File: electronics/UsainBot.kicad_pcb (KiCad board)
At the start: 2 copper layers, 176 x 198 mm, 2 parts

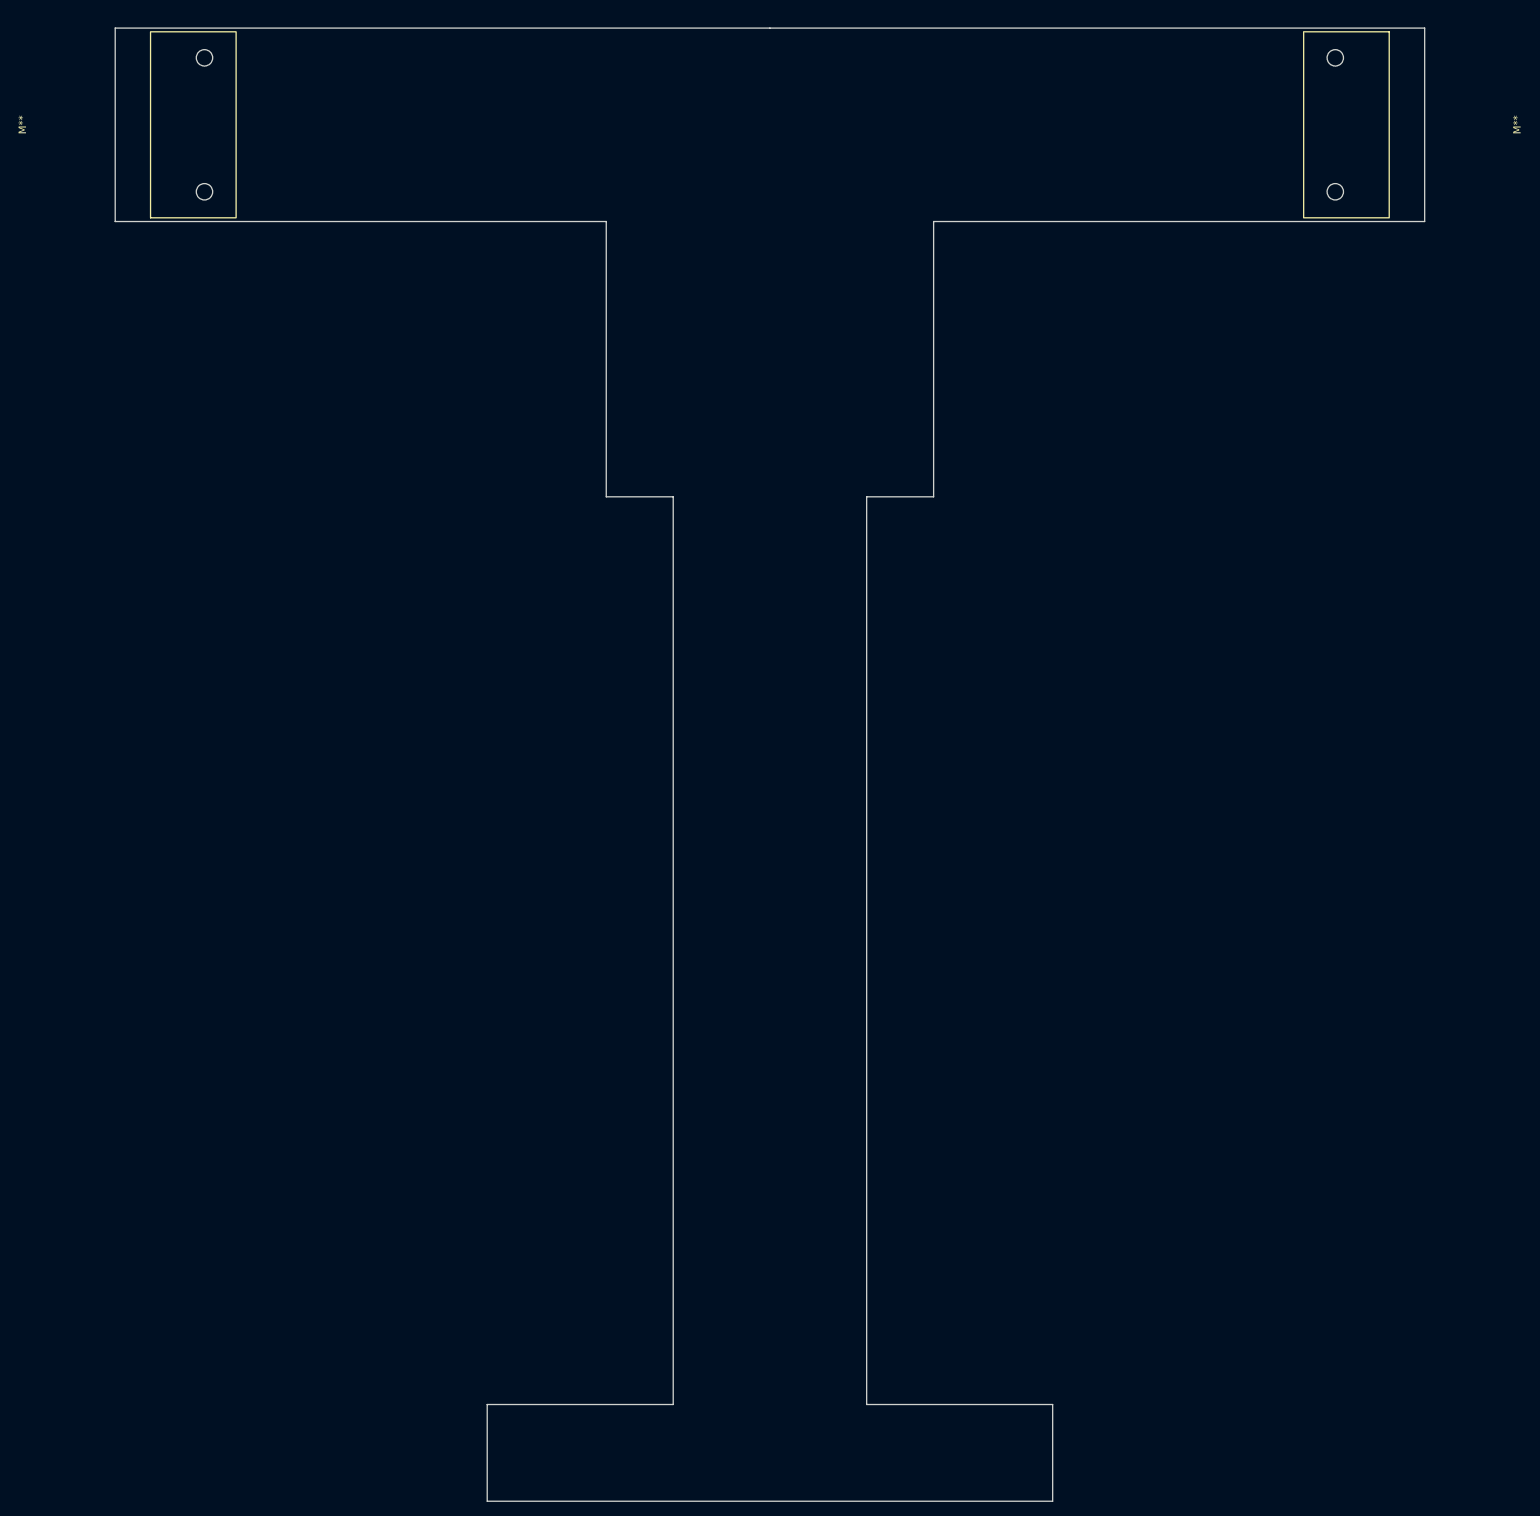
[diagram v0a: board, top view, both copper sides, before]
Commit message: Pose les 335 composants sur la carte, chacun contre l'actif qu'il sert
Le PCB ne portait que le contour. Il porte maintenant tout le schéma, placé
par script : la position de chaque composant est écrite dans `layout.py`,
jamais posée à la souris. Les rangées de résistances alignées loin de leur
circuit ont disparu ; à leur place une grappe par fonction, au contact du
boîtier. Ce qui ne pouvait pas suivre — les passifs lents des deux ponts en
H, coincés derrière l'équerre moteur — est regroupé en un bloc unique plutôt
que dispersé.

Six zones sur 194 × 155 mm. L'arrière, seule bande libre devant les
équerres, prend les ponts en H aux deux angles, le chargeur, l'USB et le
trio d'alimentation : XT30 vertical, nappe d'équilibrage, et les deux gros
perçages où se soudent les fils de l'ESC, qui se dresse sur la tranche
juste au-dessus. Le couloir entre les équerres et le trou de turbine reçoit
la centrale inertielle, au plus près du centre de rotation. Les épaules
portent le convertisseur 3,3 V — descendu là, il ne mange plus la bande
arrière —, l'interrupteur général et la station de télémétrie à 75°. L'IHM
place l'écran sur entretoises et le LQFP144 à 45° dessous, son découplage
logé dans les quatre poches entre le losange du boîtier et les bords du
module ; manettes à gauche, télémètres à droite, parce qu'on regarde l'écran
par l'arrière. Le nez enfin garde la passerelle centrale pour la station à
15°, la moustache et ses passifs étant passés dessous, contre les capteurs.

Une exception au tout-script, et elle prime : une empreinte verrouillée dans
pcbnew est une décision prise à l'écran, sur la pièce réelle. `lock_import.py`
les relève dans `locked.json`, que `layout.py` applique par-dessus sa propre
table ; `place_pcb.py` ne les efface pas au `--reset` et ne les déplace
jamais. Il rafraîchit en revanche leur dessin d'empreinte sur place —
verrouiller fige où l'on est, pas la version du plan. C'est ainsi que le
module OLED a suivi la correction d'entraxe sans bouger d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
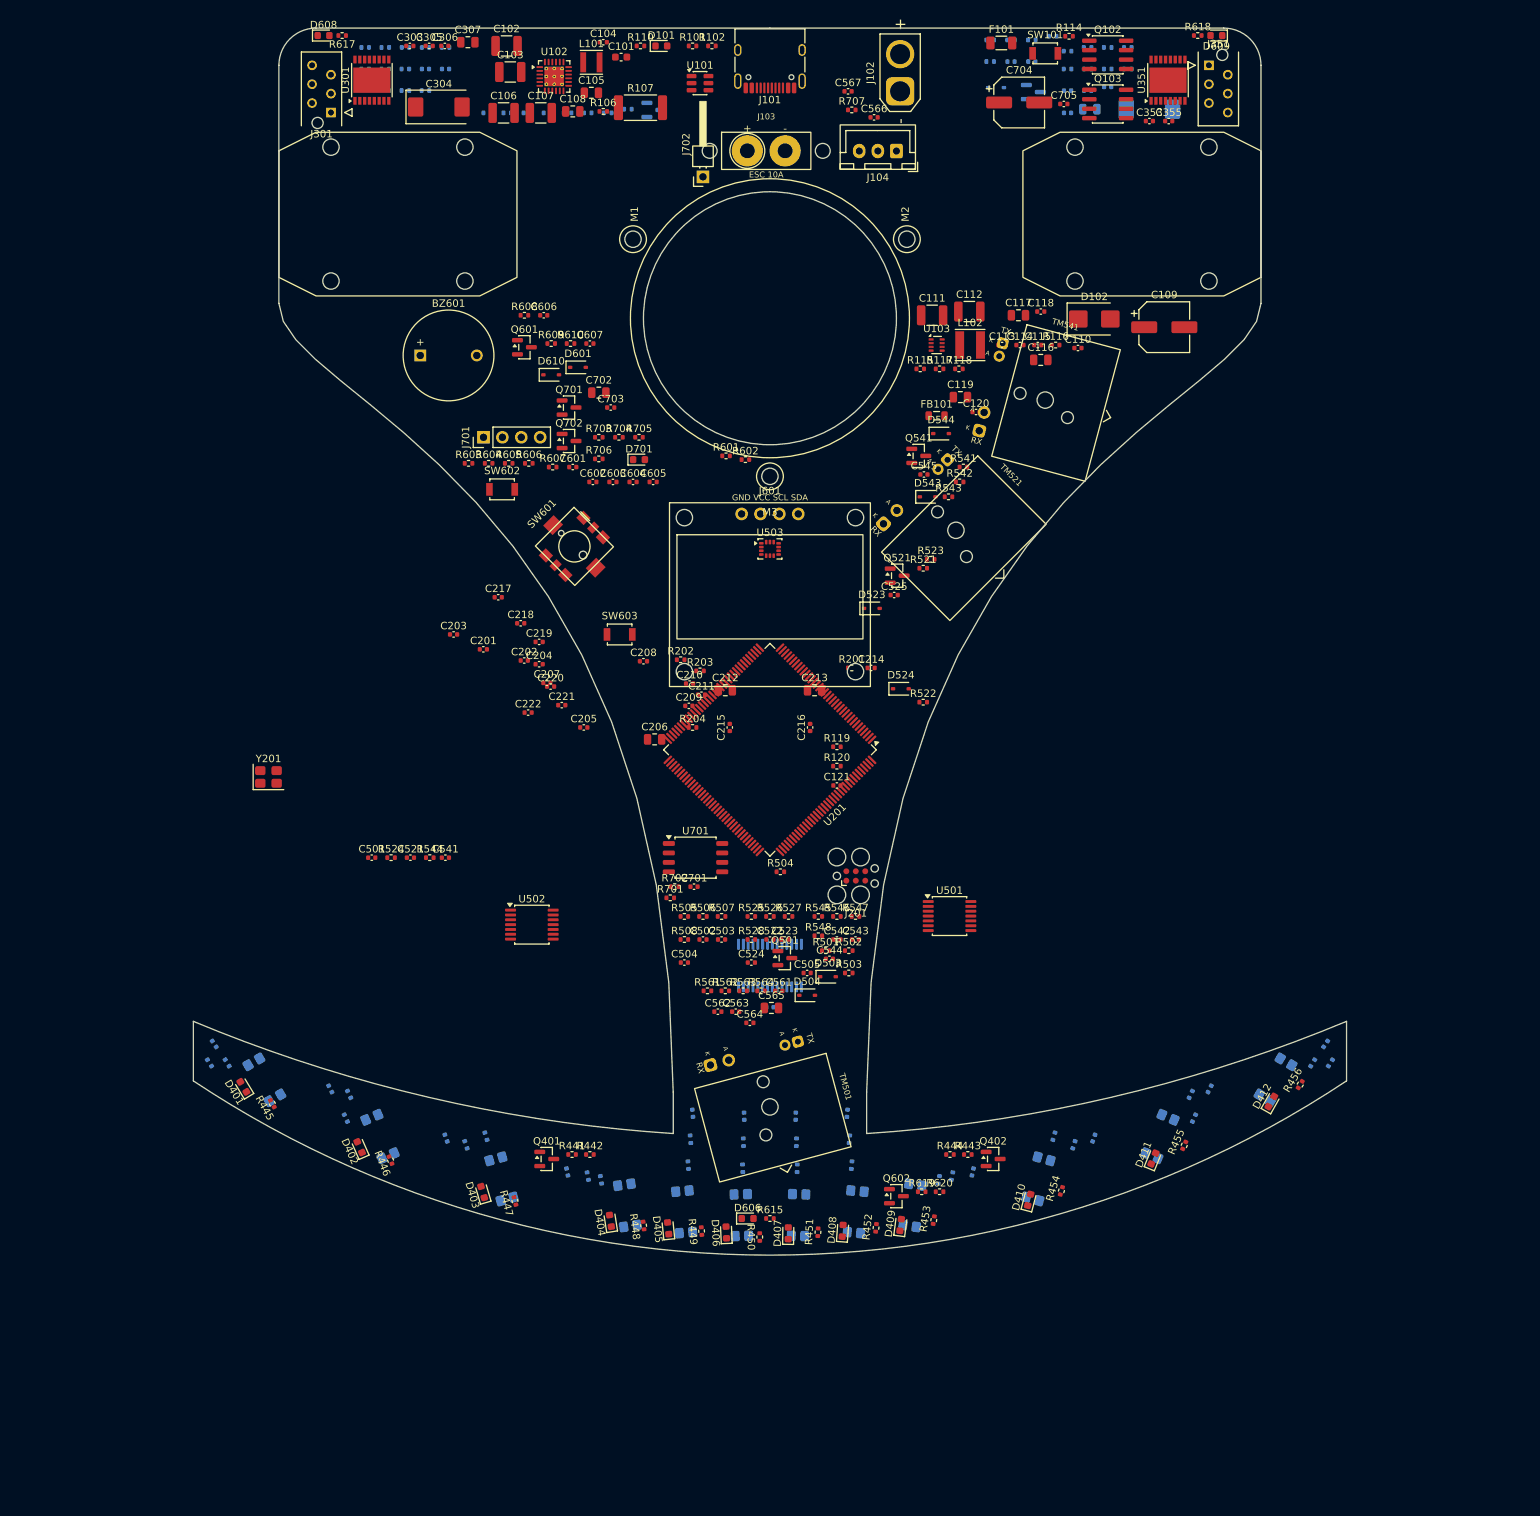
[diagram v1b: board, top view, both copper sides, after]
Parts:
- removed M** (x2): GM12-N20, Pacabot:Motor_GM12-N20_Bracket
- added BZ601: buzzer magnetique 9 x 5,5 mm, MagneticBuzzer_ProSignal_ABI-009-RC, F.Cu at (108.0, 164.0)
- added C101: 1uF, C_0603_1608Metric, F.Cu at (135.0, 123.9)
- added C102: 22uF, C_1210_3225Metric, F.Cu at (119.6, 122.4)
- added C103: 22uF, C_1210_3225Metric, F.Cu at (120.1, 125.9)
- added C104: 47nF, C_0402_1005Metric, F.Cu at (132.6, 121.9)
- added C105: 4u7F, C_0805_2012Metric, F.Cu at (131.0, 128.7)
- added C106: 22uF, C_1210_3225Metric, F.Cu at (119.2, 131.4)
- added C107: 22uF, C_1210_3225Metric, F.Cu at (124.2, 131.4)
- added C108: 10uF, C_0805_2012Metric, F.Cu at (128.5, 131.2)
- added C109: 100uF, CP_Elec_6.3x7.7, F.Cu at (208.0, 160.2)
- added C110: 100nF, C_0402_1005Metric, F.Cu at (196.4, 163.0)
- added C111: 10uF, C_1210_3225Metric, F.Cu at (176.8, 158.6)
- added C112: 10uF, C_1210_3225Metric, F.Cu at (181.8, 158.1)
- added C113: 100nF, C_0402_1005Metric, F.Cu at (186.2, 162.6)
- added C114: 100nF, C_0402_1005Metric, F.Cu at (188.6, 162.6)
- added C115: 10nF, C_0402_1005Metric, F.Cu at (191.0, 162.6)
- added C116: 22uF, C_0805_2012Metric, F.Cu at (191.4, 164.6)
- added C117: 22uF, C_0805_2012Metric, F.Cu at (188.4, 158.6)
- added C118: 100nF, C_0402_1005Metric, F.Cu at (191.4, 158.1)
- added C119: 10uF, C_0805_2012Metric, F.Cu at (180.6, 169.6)
- added C120: 100nF, C_0402_1005Metric, F.Cu at (182.7, 171.6)
- added C121: 100nF, C_0402_1005Metric, F.Cu at (164.0, 221.8)
- added C122: 100nF, C_0402_1005Metric, B.Cu at (187.4, 124.5)
- added C123: 1uF, C_0402_1005Metric, B.Cu at (190.2, 124.5)
- added C124: 100nF, C_0402_1005Metric, B.Cu at (155.0, 251.6)
- added C201: 100nF, C_0402_1005Metric, F.Cu at (116.5, 203.5)
- added C202: 100nF, C_0402_1005Metric, F.Cu at (122.0, 205.0)
- added C203: 100nF, C_0402_1005Metric, F.Cu at (112.5, 201.5)
- added C204: 100nF, C_0402_1005Metric, F.Cu at (124.0, 205.5)
- added C205: 100nF, C_0402_1005Metric, F.Cu at (130.0, 214.0)
- added C206: 4u7F, C_0805_2012Metric, F.Cu at (139.5, 215.6)
- added C207: 100nF, C_0402_1005Metric, F.Cu at (125.0, 208.0)
- added C208: 100nF, C_0402_1005Metric, F.Cu at (138.0, 205.1)
- added C209: 1uF, C_0402_1005Metric, F.Cu at (144.1, 211.1)
- added C210: 100nF, C_0402_1005Metric, F.Cu at (144.2, 208.1)
- added C211: 1uF, C_0402_1005Metric, F.Cu at (145.8, 209.6)
- added C212: 2u2F, C_0805_2012Metric, F.Cu at (149.0, 209.0)
- added C213: 2u2F, C_0805_2012Metric, F.Cu at (161.0, 209.0)
- added C214: 100nF, C_0402_1005Metric, F.Cu at (168.6, 206.0)
- added C215: 10pF, C_0402_1005Metric, F.Cu at (149.6, 214.0)
- added C216: 10pF, C_0402_1005Metric, F.Cu at (160.4, 214.0)
- added C217: 100nF, C_0402_1005Metric, F.Cu at (118.5, 196.5)
- added C218: 100nF, C_0402_1005Metric, F.Cu at (121.5, 200.0)
- added C219: 100nF, C_0402_1005Metric, F.Cu at (124.0, 202.5)
- added C220: 100nF, C_0402_1005Metric, F.Cu at (125.5, 208.5)
- added C221: 100nF, C_0402_1005Metric, F.Cu at (127.0, 211.0)
- added C222: 100nF, C_0402_1005Metric, F.Cu at (122.5, 212.0)
- added C301: 100nF, C_0402_1005Metric, B.Cu at (106.0, 122.6)
- added C302: 1nF, C_0402_1005Metric, B.Cu at (108.7, 122.6)
- added C303: 100nF, C_0402_1005Metric, F.Cu at (106.6, 122.4)
- added C304: 100uF, CP_EIA-7343-20_Kemet-V, F.Cu at (110.5, 130.6)
- added C305: 100nF, C_0402_1005Metric, F.Cu at (109.2, 122.4)
- added C306: 22nF, C_0402_1005Metric, F.Cu at (111.3, 122.4)
- added C307: 100nF, C_0805_2012Metric, F.Cu at (114.4, 121.9)
- added C308: 1nF, C_0402_1005Metric, B.Cu at (108.7, 125.5)
- added C309: 1nF, C_0402_1005Metric, B.Cu at (111.4, 125.5)
- added C352: 1nF, C_0402_1005Metric, B.Cu at (195.0, 128.4)
- added C353: 100nF, C_0402_1005Metric, F.Cu at (206.0, 132.5)
- added C354: 100uF, CP_EIA-7343-20_Kemet-V, B.Cu at (206.0, 130.9)
- added C355: 100nF, C_0402_1005Metric, F.Cu at (208.6, 132.5)
- added C356: 22nF, C_0402_1005Metric, B.Cu at (195.0, 131.4)
- added C357: 100nF, C_0805_2012Metric, B.Cu at (198.0, 130.9)
- added C358: 1nF, C_0402_1005Metric, B.Cu at (197.7, 128.4)
- added C359: 1nF, C_0402_1005Metric, B.Cu at (200.4, 127.9)
- added C401: 1nF, C_0402_1005Metric, B.Cu at (80.3, 256.5)
- added C402: 1nF, C_0402_1005Metric, B.Cu at (95.9, 262.6)
- added C403: 1nF, C_0402_1005Metric, B.Cu at (111.5, 269.2)
- added C404: 1nF, C_0402_1005Metric, B.Cu at (127.8, 273.7)
- added C405: 1nF, C_0402_1005Metric, B.Cu at (144.6, 265.9)
- added C406: 1nF, C_0402_1005Metric, B.Cu at (151.5, 266.3)
- added C407: 1nF, C_0402_1005Metric, B.Cu at (158.5, 266.3)
- added C408: 1nF, C_0402_1005Metric, B.Cu at (165.4, 265.9)
- added C409: 1nF, C_0402_1005Metric, B.Cu at (182.2, 273.7)
- added C410: 1nF, C_0402_1005Metric, B.Cu at (198.5, 269.2)
- added C411: 1nF, C_0402_1005Metric, B.Cu at (214.1, 262.6)
- added C412: 1nF, C_0402_1005Metric, B.Cu at (229.7, 256.5)
- added C501: 22pF, C_0402_1005Metric, F.Cu at (101.5, 231.5)
- added C502: 1nF, C_0402_1005Metric, F.Cu at (146.0, 242.5)
- added C503: 1uF, C_0402_1005Metric, F.Cu at (148.5, 242.5)
- added C504: 4n7, C_0402_1005Metric, F.Cu at (143.5, 245.6)
- added C505: 10nF, C_0402_1005Metric, F.Cu at (160.0, 247.0)
- added C521: 22pF, C_0402_1005Metric, F.Cu at (106.7, 231.5)
- added C522: 1nF, C_0402_1005Metric, F.Cu at (155.0, 242.5)
- added C523: 1uF, C_0402_1005Metric, F.Cu at (157.0, 242.5)
- added C524: 4n7, C_0402_1005Metric, F.Cu at (152.5, 245.6)
- added C525: 10nF, C_0402_1005Metric, F.Cu at (171.7, 196.2)
- added C541: 22pF, C_0402_1005Metric, F.Cu at (111.4, 231.5)
- added C542: 1nF, C_0402_1005Metric, F.Cu at (164.0, 242.5)
- added C543: 1uF, C_0402_1005Metric, F.Cu at (166.5, 242.5)
- added C544: 4n7, C_0402_1005Metric, F.Cu at (163.0, 245.1)
- added C545: 10nF, C_0402_1005Metric, F.Cu at (175.7, 180.0)
- added C561: 1uF, C_0402_1005Metric, F.Cu at (156.2, 249.4)
- added C562: 1uF, C_0402_1005Metric, F.Cu at (148.0, 252.2)
- added C563: 100nF, C_0402_1005Metric, F.Cu at (150.4, 252.2)
- added C564: 100nF, C_0402_1005Metric, F.Cu at (152.3, 253.7)
- added C565: 10uF, C_0805_2012Metric, F.Cu at (155.2, 251.7)
- added C566: 100nF, C_0402_1005Metric, F.Cu at (169.0, 132.0)
- added C567: 100nF, C_0402_1005Metric, F.Cu at (165.5, 128.5)
- added C601: 100nF, C_0402_1005Metric, F.Cu at (128.5, 179.0)
- added C602: 100nF, C_0402_1005Metric, F.Cu at (131.2, 181.0)
- added C603: 100nF, C_0402_1005Metric, F.Cu at (133.9, 181.0)
- added C604: 100nF, C_0402_1005Metric, F.Cu at (136.6, 181.0)
- added C605: 100nF, C_0402_1005Metric, F.Cu at (139.3, 181.0)
- added C606: 100nF, C_0402_1005Metric, F.Cu at (124.6, 158.6)
- added C607: 100nF, C_0402_1005Metric, F.Cu at (130.8, 162.4)
- added C701: 100nF, C_0402_1005Metric, F.Cu at (144.8, 235.4)
- added C702: 10uF, C_0805_2012Metric, F.Cu at (132.0, 169.0)
- added C703: 100nF, C_0402_1005Metric, F.Cu at (133.6, 171.0)
- added C704: 220uF, CP_Elec_6.3x7.7, F.Cu at (188.5, 130.0)
- added C705: 100nF, C_0402_1005Metric, F.Cu at (194.5, 130.2)
- added D101: vert - charge, LED_0603_1608Metric, F.Cu at (140.4, 122.4)
- added D102: SMBJ9.0A, D_SMB, F.Cu at (198.6, 159.1)
- added D106: BAT54, D_SOD-323, B.Cu at (185.4, 128.0)
- added D401: verte - capteur 00, LED_0603_1608Metric, F.Cu at (84.2, 262.3)
- added D402: verte - capteur 01, LED_0603_1608Metric, F.Cu at (99.9, 270.4)
- added D403: verte - capteur 02, LED_0603_1608Metric, F.Cu at (116.4, 276.4)
- added D404: verte - capteur 03, LED_0603_1608Metric, F.Cu at (133.6, 280.3)
- added D405: verte - capteur 04, LED_0603_1608Metric, F.Cu at (141.3, 281.3)
- added D406: verte - capteur 05, LED_0603_1608Metric, F.Cu at (149.1, 281.9)
- added D407: verte - capteur 06, LED_0603_1608Metric, F.Cu at (157.5, 282.0)
- added D408: verte - capteur 07, LED_0603_1608Metric, F.Cu at (164.8, 281.7)
- added D409: verte - capteur 08, LED_0603_1608Metric, F.Cu at (172.6, 280.9)
- added D410: verte - capteur 09, LED_0603_1608Metric, F.Cu at (189.8, 277.5)
- added D411: verte - capteur 10, LED_0603_1608Metric, F.Cu at (206.5, 271.9)
- added D412: verte - capteur 11, LED_0603_1608Metric, F.Cu at (222.4, 264.3)
- added D503: PESD3V3, D_SOD-323, F.Cu at (162.8, 247.5)
- added D504: BAT54, D_SOD-323, F.Cu at (160.0, 250.0)
- added D523: PESD3V3, D_SOD-323, F.Cu at (168.7, 198.0)
- added D524: BAT54, D_SOD-323, F.Cu at (172.6, 208.8)
- added D543: PESD3V3, D_SOD-323, F.Cu at (176.2, 183.0)
- added D544: BAT54, D_SOD-323, F.Cu at (178.0, 174.5)
- added D601: BAT54, D_SOD-323, F.Cu at (129.2, 165.6)
- added D606: bleue - nez, LED_0603_1608Metric, F.Cu at (152.0, 280.0)
- added D608: rouge - arriere, LED_0603_1608Metric, F.Cu at (95.0, 121.0)
- added D609: rouge - arriere, LED_0603_1608Metric, F.Cu at (215.0, 121.0)
- added D610: BAT54, D_SOD-323, F.Cu at (125.6, 166.6)
- added D701: bleue, LED_0603_1608Metric, F.Cu at (137.4, 178.0)
- added F101: 12 A, R_1206_3216Metric, F.Cu at (186.1, 122.0)
- added FB101: 600R @ 100 MHz, L_0805_2012Metric, F.Cu at (177.4, 172.1)
- added J101: TYPE-C-31-M-12, USB_C_Receptacle_HRO_TYPE-C-31-M-12, F.Cu at (155.0, 124.0)
- added J102: Pack 2S - puissance, AMASS_XT30U-M_1x02_P5.0mm_Vertical, F.Cu at (172.5, 128.5)
- added J103: MultiStar 10A (debout), Pacabot:ESC_Multistar_10A, F.Cu at (154.5, 136.5)
- added J104: Pack 2S - equilibrage, JST_XH_B3B-XH-A_1x03_P2.50mm_Vertical, F.Cu at (172.0, 136.5)
- added J201: TC2030-IDC-FP, Tag-Connect_TC2030-IDC-FP_2x03_P1.27mm_Vertical, F.Cu at (166.5, 234.0)
- added J301: Moteur Faulhaber + IE2, TE_Micro-MaTch_215079-6_2x03_P1.27mm_Vertical, F.Cu at (96.0, 131.3)
- added J351: Moteur Faulhaber + IE2, TE_Micro-MaTch_215079-6_2x03_P1.27mm_Vertical, F.Cu at (214.0, 125.0)
- added J601: OLED SSD1306 I2C, OLED_096_I2C, F.Cu at (155.0, 196.2)
- added J701: Module OTA (ESP32-C3), PinHeader_1x04_P2.54mm_Vertical, F.Cu at (116.5, 175.0)
- added J702: Signal ESC (coudee), PinHeader_1x01_P2.54mm_Horizontal, F.Cu at (146.0, 140.0)
- added L101: 1uH / 4 A, L_Taiyo-Yuden_NR-30xx, F.Cu at (131.0, 124.6)
- added L102: 4u7H / 3 A, L_Taiyo-Yuden_NR-40xx, F.Cu at (181.9, 162.6)
- added M1: Faulhaber 1524T006SR + IE2 + 15/10, Motor_Faulhaber_1524_15-10, F.Cu at (105.0, 145.0)
- added M2: Faulhaber 1524T006SR + IE2 + 15/10, Motor_Faulhaber_1524_15-10, F.Cu at (205.0, 145.0)
- added M3: Turbine_EDF27_dessus, Turbine_EDF27_dessus, F.Cu at (155.0, 159.0)
- added Q101: AO3400A, SOT-23, B.Cu at (139.4, 131.0)
- added Q102: AO4407A, SOIC-8_3.9x4.9mm_P1.27mm, F.Cu at (200.4, 123.6)
- added Q103: AO4407A, SOIC-8_3.9x4.9mm_P1.27mm, F.Cu at (200.4, 130.2)
- added Q104: AO3400A, SOT-23, B.Cu at (190.4, 128.6)
- added Q401: AO3400A, SOT-23, F.Cu at (125.0, 272.0)
- added Q402: AO3400A, SOT-23, F.Cu at (185.0, 272.0)
- added Q501: AO3400A, SOT-23, F.Cu at (157.0, 245.0)
- added Q521: AO3400A, SOT-23, F.Cu at (172.1, 193.6)
- added Q541: AO3400A, SOT-23, F.Cu at (175.0, 177.5)
- added Q601: AO3400A, SOT-23, F.Cu at (122.0, 162.9)
- added Q602: AO3400A, SOT-23, F.Cu at (172.0, 277.0)
- added Q701: SI2301CDS, SOT-23, F.Cu at (128.0, 171.0)
- added Q702: AO3400A, SOT-23, F.Cu at (128.0, 175.5)
- added R101: 5k1, R_0402_1005Metric, F.Cu at (144.6, 122.4)
- added R102: 5k1, R_0402_1005Metric, F.Cu at (147.2, 122.4)
- added R103: 383R, R_0402_1005Metric, B.Cu at (117.0, 131.4)
- added R104: 5k23, R_0402_1005Metric, B.Cu at (119.7, 131.4)
- added R105: 30k1, R_0402_1005Metric, B.Cu at (122.4, 131.4)
- added R106: 300R, R_0402_1005Metric, F.Cu at (132.6, 131.2)
- added R107: 10R, R_2512_6332Metric, F.Cu at (137.6, 130.7)
- added R108: 10k, R_0402_1005Metric, B.Cu at (125.1, 131.4)
- added R109: 10k, R_0402_1005Metric, B.Cu at (127.8, 131.4)
- added R110: 2k2, R_0402_1005Metric, F.Cu at (137.6, 122.4)
- added R111: 100k, R_0402_1005Metric, B.Cu at (130.5, 131.4)
- added R112: 100R, R_0402_1005Metric, B.Cu at (133.2, 131.4)
- added R113: 100k, R_0402_1005Metric, B.Cu at (135.9, 130.9)
- added R114: 100k, R_0402_1005Metric, F.Cu at (195.2, 121.1)
- added R115: 100k, R_0402_1005Metric, F.Cu at (175.2, 165.8)
- added R116: 42k2, R_0402_1005Metric, F.Cu at (193.4, 162.6)
- added R117: 100k, R_0402_1005Metric, F.Cu at (177.8, 165.8)
- added R118: 31k6, R_0402_1005Metric, F.Cu at (180.4, 165.8)
- added R119: 22k, R_0402_1005Metric, F.Cu at (164.0, 216.6)
- added R120: 10k, R_0402_1005Metric, F.Cu at (164.0, 219.2)
- added R124: 100R, R_0402_1005Metric, B.Cu at (184.6, 121.6)
- added R125: 10k, R_0402_1005Metric, B.Cu at (187.4, 121.6)
- added R126: 100k, R_0402_1005Metric, B.Cu at (190.2, 121.6)
- added R127: 470k, R_0402_1005Metric, B.Cu at (193.0, 121.1)
- added R128: 220k, R_0402_1005Metric, B.Cu at (184.6, 124.5)
- added R201: 10k, R_0402_1005Metric, F.Cu at (166.0, 206.0)
- added R202: 10k, R_0402_1005Metric, F.Cu at (143.0, 204.9)
- added R203: 10k, R_0402_1005Metric, F.Cu at (145.6, 206.4)
- added R204: 220R, R_0402_1005Metric, F.Cu at (144.6, 214.0)
- added R301: 10k, R_0402_1005Metric, B.Cu at (100.6, 122.6)
- added R302: 6k8, R_0402_1005Metric, B.Cu at (103.3, 122.6)
- added R303: 100k, R_0402_1005Metric, B.Cu at (111.4, 122.6)
- added R304: 10k, R_0402_1005Metric, B.Cu at (100.6, 125.5)
- added R305: 20k, R_0402_1005Metric, B.Cu at (103.3, 125.5)
- added R306: 10k, R_0402_1005Metric, B.Cu at (106.0, 125.5)
- added R307: 1k, R_0402_1005Metric, B.Cu at (100.6, 128.4)
- added R308: 100R, R_0402_1005Metric, B.Cu at (103.3, 128.4)
- added R309: 100R, R_0402_1005Metric, B.Cu at (106.0, 128.4)
- added R310: 100R, R_0402_1005Metric, B.Cu at (108.7, 128.4)
- added R353: 100k, R_0402_1005Metric, B.Cu at (195.0, 123.1)
- added R354: 10k, R_0402_1005Metric, B.Cu at (197.7, 122.6)
- added R355: 20k, R_0402_1005Metric, B.Cu at (200.4, 122.6)
- added R356: 10k, R_0402_1005Metric, B.Cu at (203.1, 122.6)
- added R357: 1k, R_0402_1005Metric, B.Cu at (195.0, 125.5)
- added R358: 100R, R_0402_1005Metric, B.Cu at (197.7, 125.5)
- added R359: 100R, R_0402_1005Metric, B.Cu at (200.4, 125.5)
- added R360: 100R, R_0402_1005Metric, B.Cu at (203.1, 125.5)
- added R401: 100R, R_0402_1005Metric, B.Cu at (82.0, 259.1)
- added R402: 100R, R_0402_1005Metric, B.Cu at (98.0, 266.5)
- added R403: 100R, R_0402_1005Metric, B.Cu at (116.8, 268.9)
- added R404: 100R, R_0402_1005Metric, B.Cu at (132.3, 274.8)
- added R405: 100R, R_0402_1005Metric, B.Cu at (144.0, 272.8)
- added R406: 100R, R_0402_1005Metric, B.Cu at (151.3, 273.2)
- added R407: 100R, R_0402_1005Metric, B.Cu at (158.7, 273.2)
- added R408: 100R, R_0402_1005Metric, B.Cu at (166.0, 272.8)
- added R409: 100R, R_0402_1005Metric, B.Cu at (177.7, 274.8)
- added R410: 100R, R_0402_1005Metric, B.Cu at (193.2, 268.9)
- added R411: 100R, R_0402_1005Metric, B.Cu at (212.0, 266.5)
- added R412: 100R, R_0402_1005Metric, B.Cu at (227.9, 259.1)
- added R421: 10k, R_0402_1005Metric, B.Cu at (79.7, 259.1)
- added R422: 10k, R_0402_1005Metric, B.Cu at (98.4, 263.3)
- added R423: 10k, R_0402_1005Metric, B.Cu at (114.1, 270.1)
- added R424: 10k, R_0402_1005Metric, B.Cu at (130.5, 274.3)
- added R425: 10k, R_0402_1005Metric, B.Cu at (144.3, 269.3)
- added R426: 10k, R_0402_1005Metric, B.Cu at (151.4, 269.7)
- added R427: 10k, R_0402_1005Metric, B.Cu at (158.6, 269.7)
- added R428: 10k, R_0402_1005Metric, B.Cu at (165.7, 269.3)
- added R429: 10k, R_0402_1005Metric, B.Cu at (179.5, 274.3)
- added R430: 10k, R_0402_1005Metric, B.Cu at (195.9, 270.1)
- added R431: 10k, R_0402_1005Metric, B.Cu at (211.6, 263.3)
- added R432: 10k, R_0402_1005Metric, B.Cu at (230.3, 259.1)
- added R441: 100R, R_0402_1005Metric, F.Cu at (128.4, 271.4)
- added R442: 100k, R_0402_1005Metric, F.Cu at (130.8, 271.4)
- added R443: 100R, R_0402_1005Metric, F.Cu at (181.6, 271.4)
- added R444: 100k, R_0402_1005Metric, F.Cu at (179.2, 271.4)
- added R445: 1k, R_0402_1005Metric, F.Cu at (88.1, 264.6)
- added R446: 1k, R_0402_1005Metric, F.Cu at (104.0, 272.2)
- added R447: 1k, R_0402_1005Metric, F.Cu at (120.7, 277.6)
- added R448: 1k, R_0402_1005Metric, F.Cu at (138.0, 280.9)
- added R449: 1k, R_0402_1005Metric, F.Cu at (145.8, 281.7)
- added R450: 1k, R_0402_1005Metric, F.Cu at (153.6, 282.5)
- added R451: 1k, R_0402_1005Metric, F.Cu at (161.5, 281.8)
- added R452: 1k, R_0402_1005Metric, F.Cu at (169.3, 281.3)
- added R453: 1k, R_0402_1005Metric, F.Cu at (177.0, 280.2)
- added R454: 1k, R_0402_1005Metric, F.Cu at (194.2, 276.3)
- added R455: 1k, R_0402_1005Metric, F.Cu at (210.7, 270.2)
- added R456: 1k, R_0402_1005Metric, F.Cu at (226.3, 262.0)
- added R501: 100R, R_0402_1005Metric, F.Cu at (162.5, 244.0)
- added R502: 100R, R_0402_1005Metric, F.Cu at (165.6, 244.0)
- added R503: 100k, R_0402_1005Metric, F.Cu at (165.6, 247.0)
- added R504: 220k, R_0402_1005Metric, F.Cu at (156.4, 233.4)
- added R505: 100k, R_0402_1005Metric, F.Cu at (143.5, 239.4)
- added R506: 100k, R_0402_1005Metric, F.Cu at (146.0, 239.4)
- added R507: 910R, R_0402_1005Metric, F.Cu at (148.5, 239.4)
- added R508: 1k, R_0402_1005Metric, F.Cu at (143.5, 242.5)
- added R521: 100R, R_0402_1005Metric, F.Cu at (175.6, 192.6)
- added R522: 100R, R_0402_1005Metric, F.Cu at (175.6, 210.6)
- added R523: 100k, R_0402_1005Metric, F.Cu at (176.6, 191.4)
- added R524: 220k, R_0402_1005Metric, F.Cu at (104.1, 231.5)
- added R525: 100k, R_0402_1005Metric, F.Cu at (152.5, 239.4)
- added R526: 100k, R_0402_1005Metric, F.Cu at (155.0, 239.4)
- added R527: 910R, R_0402_1005Metric, F.Cu at (157.5, 239.4)
- added R528: 1k, R_0402_1005Metric, F.Cu at (152.5, 242.5)
- added R541: 100R, R_0402_1005Metric, F.Cu at (181.0, 179.0)
- added R542: 100R, R_0402_1005Metric, F.Cu at (180.5, 181.0)
- added R543: 100k, R_0402_1005Metric, F.Cu at (179.0, 183.0)
- added R544: 220k, R_0402_1005Metric, F.Cu at (109.3, 231.5)
- added R545: 100k, R_0402_1005Metric, F.Cu at (161.5, 239.4)
- added R546: 100k, R_0402_1005Metric, F.Cu at (164.0, 239.4)
- added R547: 910R, R_0402_1005Metric, F.Cu at (166.5, 239.4)
- added R548: 1k, R_0402_1005Metric, F.Cu at (161.5, 242.0)
- added R561: 10k, R_0402_1005Metric, F.Cu at (146.6, 249.4)
- added R562: 2k2, R_0402_1005Metric, F.Cu at (149.0, 249.4)
- added R563: 10k, R_0402_1005Metric, F.Cu at (151.4, 249.4)
- added R564: 10k, R_0402_1005Metric, F.Cu at (153.8, 249.4)
- added R601: 4k7, R_0402_1005Metric, F.Cu at (149.1, 177.5)
- added R602: 4k7, R_0402_1005Metric, F.Cu at (151.7, 178.0)
- added R603: 10k, R_0402_1005Metric, F.Cu at (114.5, 178.5)
- added R604: 10k, R_0402_1005Metric, F.Cu at (117.2, 178.5)
- added R605: 10k, R_0402_1005Metric, F.Cu at (119.9, 178.5)
- added R606: 10k, R_0402_1005Metric, F.Cu at (122.6, 178.5)
- added R607: 10k, R_0402_1005Metric, F.Cu at (125.8, 179.0)
- added R608: 10k, R_0402_1005Metric, F.Cu at (122.0, 158.6)
- added R609: 100R, R_0402_1005Metric, F.Cu at (125.6, 162.4)
- added R610: 100k, R_0402_1005Metric, F.Cu at (128.2, 162.4)
- added R615: 220R, R_0402_1005Metric, F.Cu at (155.0, 280.0)
- added R617: 300R, R_0402_1005Metric, F.Cu at (97.5, 121.0)
- added R618: 300R, R_0402_1005Metric, F.Cu at (212.5, 121.0)
- added R619: 100R, R_0402_1005Metric, F.Cu at (175.4, 276.4)
- added R620: 100k, R_0402_1005Metric, F.Cu at (177.8, 276.4)
- added R701: 10k, R_0402_1005Metric, F.Cu at (141.6, 236.9)
- added R702: 10k, R_0402_1005Metric, F.Cu at (142.2, 235.4)
- added R703: 100k, R_0402_1005Metric, F.Cu at (132.0, 175.0)
- added R704: 100R, R_0402_1005Metric, F.Cu at (134.7, 175.0)
- added R705: 100k, R_0402_1005Metric, F.Cu at (137.4, 175.0)
- added R706: 1k, R_0402_1005Metric, F.Cu at (132.0, 177.9)
- added R707: 100R, R_0402_1005Metric, F.Cu at (166.0, 131.0)
- added SW101: MARCHE / ARRET, SW_SPST_B3U-1000P, F.Cu at (192.0, 123.4)
- added SW601: SKRHABE010, SKRHABE010, F.Cu at (128.7, 189.7)
- added SW602: START, SW_SPST_B3U-1000P, F.Cu at (119.0, 182.0)
- added SW603: RESET, SW_SPST_B3U-1000P, F.Cu at (134.8, 201.5)
- added TM501: OPV302 + BPV10NF, Telemetry_Duo_Coude, F.Cu at (155.0, 265.0)
- added TM521: OPV302 + BPV10NF, Telemetry_Duo_Coude, F.Cu at (180.0, 187.5)
- added TM541: OPV302 + BPV10NF, Telemetry_Duo_Coude, F.Cu at (192.0, 170.0)
- added U101: USBLC6-2SC6, SOT-23-6, F.Cu at (145.6, 127.4)
- added U102: BQ25887RGER, HVQFN-24-1EP_4x4mm_P0.5mm_EP2.6x2.6mm_ThermalVias, F.Cu at (126.0, 126.5)
- added U103: TPS62933DRLR, SOT-583-8, F.Cu at (177.4, 162.6)
- added U105: PCA9685PW, TSSOP-28_4.4x9.7mm_P0.65mm, B.Cu at (155.0, 246.0)
- added U201: STM32H723ZGT6, LQFP-144_20x20mm_P0.5mm, F.Cu at (155.0, 217.0)
- added U301: DRV8874PWPR, HTSSOP-16-1EP_4.4x5mm_P0.65mm_EP3.4x5mm, F.Cu at (101.5, 127.0)
- added U351: DRV8874PWPR, HTSSOP-16-1EP_4.4x5mm_P0.65mm_EP3.4x5mm, F.Cu at (208.5, 127.0)
- added U401: ITR8307/S17/TR8, ITR8307_dessous, B.Cu at (87.0, 261.4)
- added U402: ITR8307/S17/TR8, ITR8307_dessous, B.Cu at (102.6, 269.0)
- added U403: ITR8307/S17/TR8, ITR8307_dessous, B.Cu at (118.9, 274.7)
- added U404: ITR8307/S17/TR8, ITR8307_dessous, B.Cu at (135.8, 278.2)
- added U405: ITR8307/S17/TR8, ITR8307_dessous, B.Cu at (143.5, 279.1)
- added U406: ITR8307/S17/TR8, ITR8307_dessous, B.Cu at (151.2, 279.5)
- added U407: ITR8307/S17/TR8, ITR8307_dessous, B.Cu at (158.8, 279.5)
- added U408: ITR8307/S17/TR8, ITR8307_dessous, B.Cu at (166.5, 279.1)
- added U409: ITR8307/S17/TR8, ITR8307_dessous, B.Cu at (174.2, 278.2)
- added U410: ITR8307/S17/TR8, ITR8307_dessous, B.Cu at (191.1, 274.7)
- added U411: ITR8307/S17/TR8, ITR8307_dessous, B.Cu at (207.4, 269.0)
- added U412: ITR8307/S17/TR8, ITR8307_dessous, B.Cu at (223.0, 261.4)
- added U501: TLV9064, TSSOP-14_4.4x5mm_P0.65mm, F.Cu at (179.1, 239.3)
- added U502: TLV9064, TSSOP-14_4.4x5mm_P0.65mm, F.Cu at (123.0, 240.5)
- added U503: LSM6DSOTR, LGA-14_3x2.5mm_P0.5mm_LayoutBorder3x4y, F.Cu at (155.0, 190.0)
- added U701: W25Q128JVSIQ, SOIC-8_5.3x5.3mm_P1.27mm, F.Cu at (145.0, 231.5)
- added Y201: 25 MHz / 10 ppm, Crystal_SMD_3225-4Pin_3.2x2.5mm, F.Cu at (87.6, 220.7)
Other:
- board size 176 x 198 mm -> 155 x 164.9 mm
- copper layers 2 -> 4
